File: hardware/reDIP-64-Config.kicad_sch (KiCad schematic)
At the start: 19 parts, among them J2 Conn_02x05_Odd_Even, SW1 KXT331LHS, U14 W957A8MFYA5I, U15 W25Q128JVPIM, U8 LFE5UM5G-25F-8MG285C

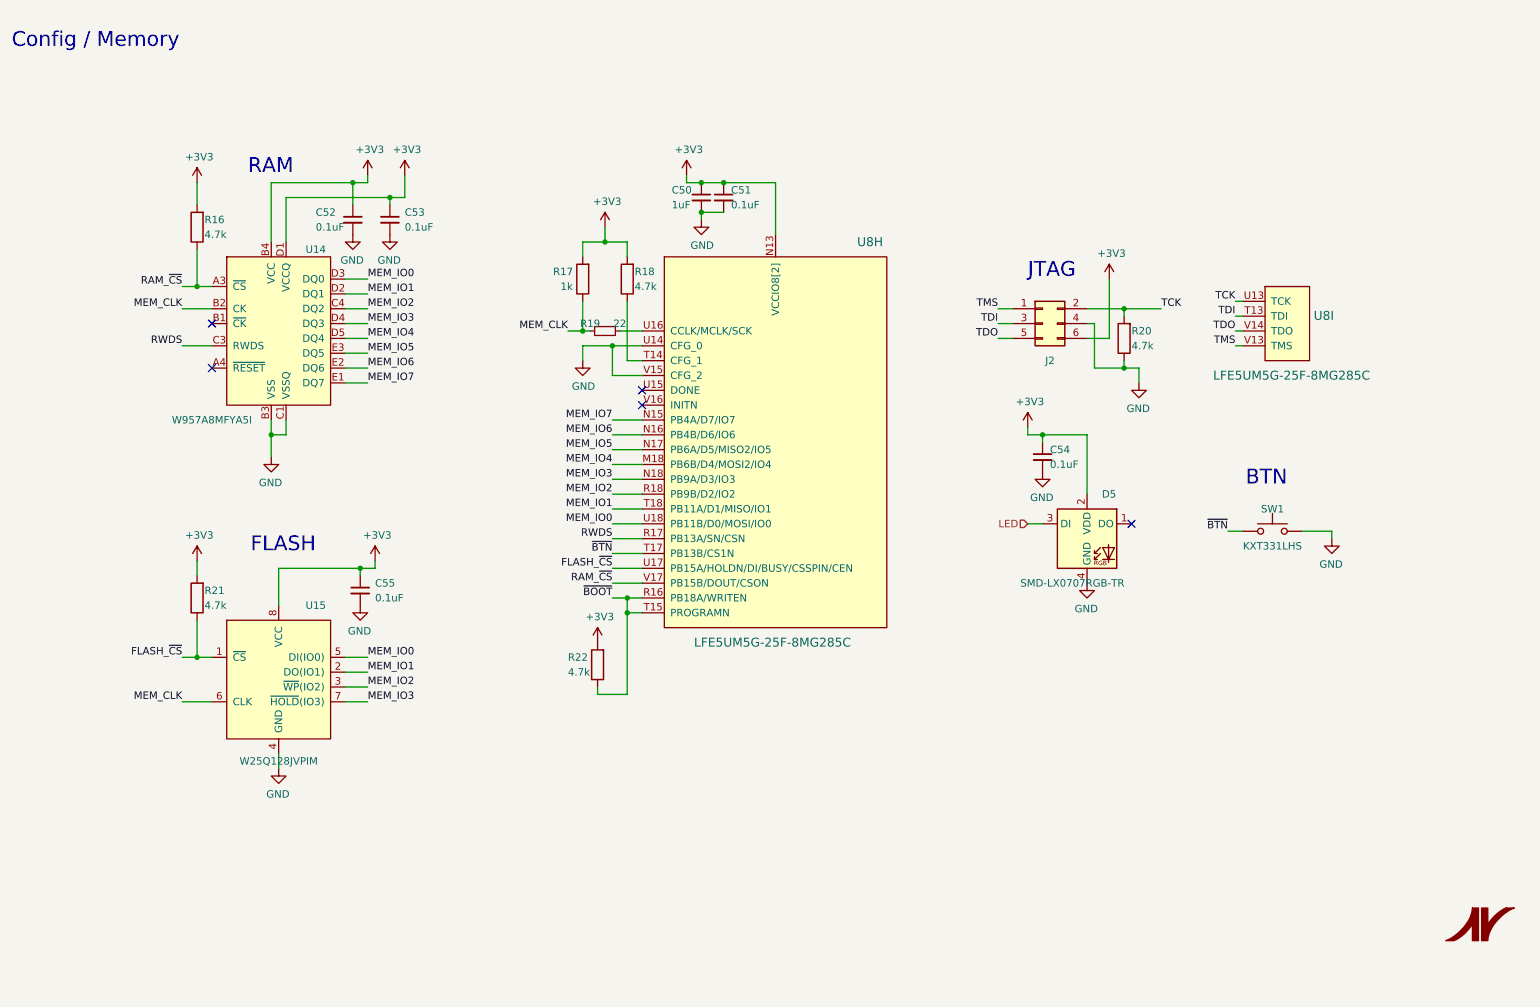
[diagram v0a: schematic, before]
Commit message: Various improvements
* Removed slash from sheet names
* Reannotated schematics
* Example derivation of clocks in schematics
* Identical capacitors for DisplayPort main lanes and AUX
* Replaced switch FSA2259UMX with FSUSB42UMX
* Modified PCB physical stackup to (hopefully) be manufacturable
* Only one microvia size (0.1mm)
* Changed track width for differential pairs
* Routing cleanups and improvements
* Added files for manufacture
* Updated README

Many thanks for advice and help go to @azonenberg, @DX-MON, @gatecat,
@smunaut, and @zyp.
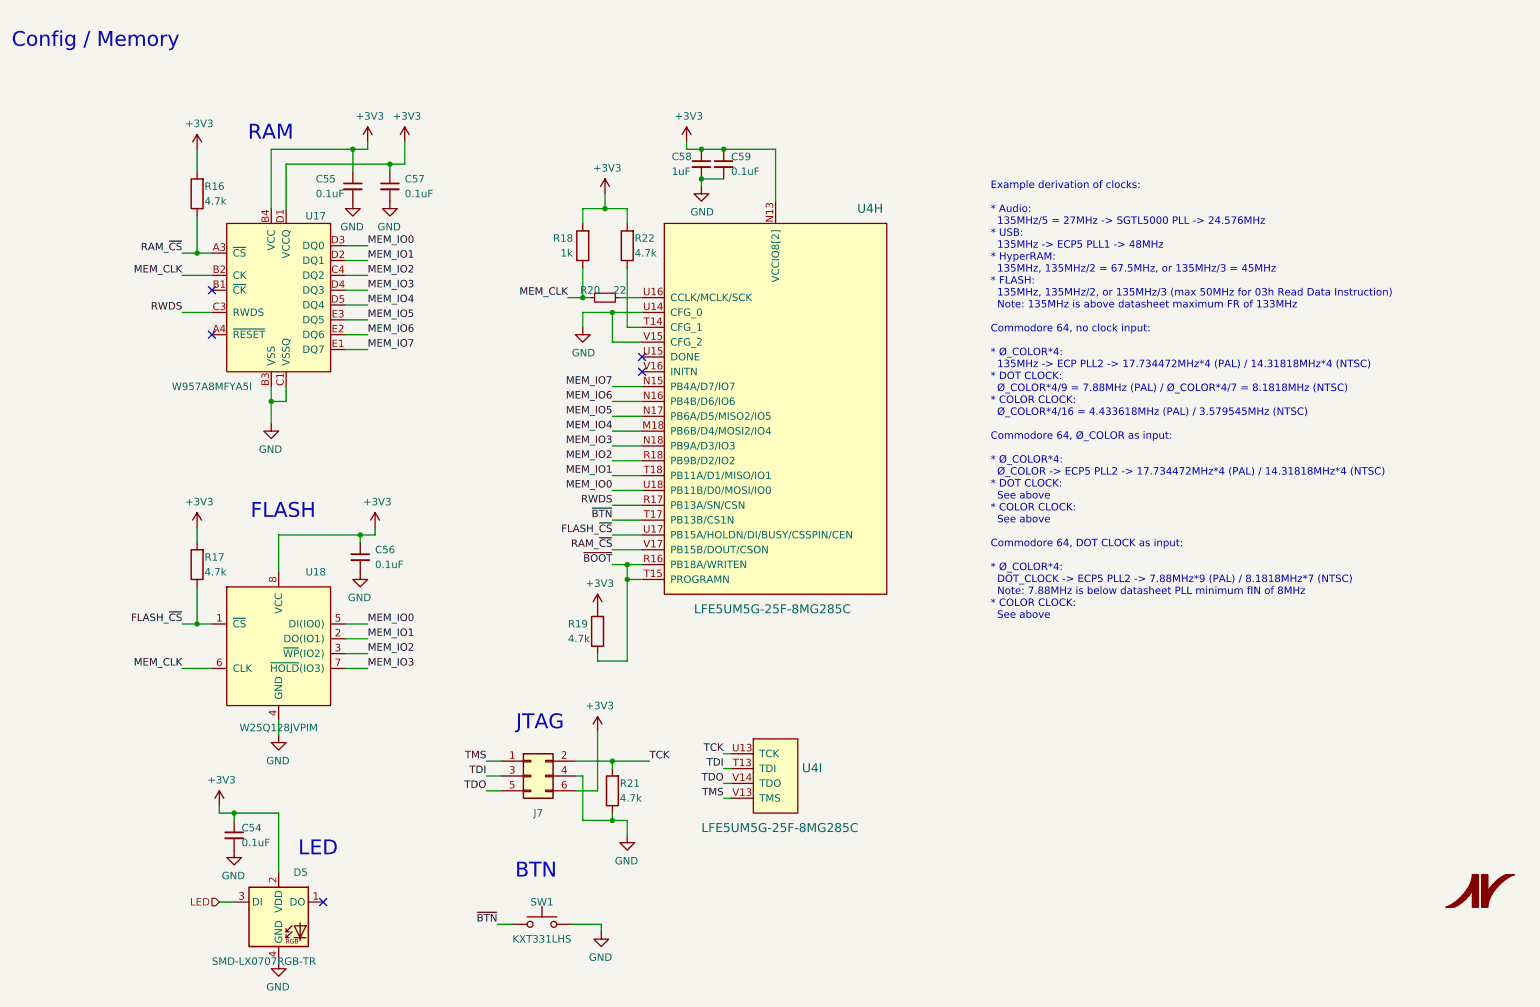
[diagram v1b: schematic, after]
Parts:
- renumbered C52 to C55, C55 to C56, C53 to C57, C50 to C58, C51 to C59, J2 to J7, R21 to R17, R17 to R18, R22 to R19, R19 to R20, R20 to R21, R18 to R22, U14 to U17, U15 to U18, U8 to U4
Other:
- note added: "Example derivation of clocks: * Audio: 135MHz/5 = 27MHz -> SGTL5000 PLL -> 24.576MHz * USB: 135MHz -> ECP5 PLL1 -> 48MHz * HyperRAM: 135MHz, 135MHz/2 = 67.5MHz, or 135MHz/3 = 45MHz * FLASH: 135MHz, 135MHz/2, or 135MHz/3 (max 50MHz for 03h Read Data Instruction) Note: 135MHz is above datasheet maximum FR of 133MHz Commodore 64, no clock input: * Ø_COLOR*4: 135MHz -> ECP PLL2 -> 17.734472MHz*4 (PAL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"
- note added: "LED"
- moved on the sheet: C54, C55, C56, C57, C58, C59, D5, J7, R16, R17, R18, R19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

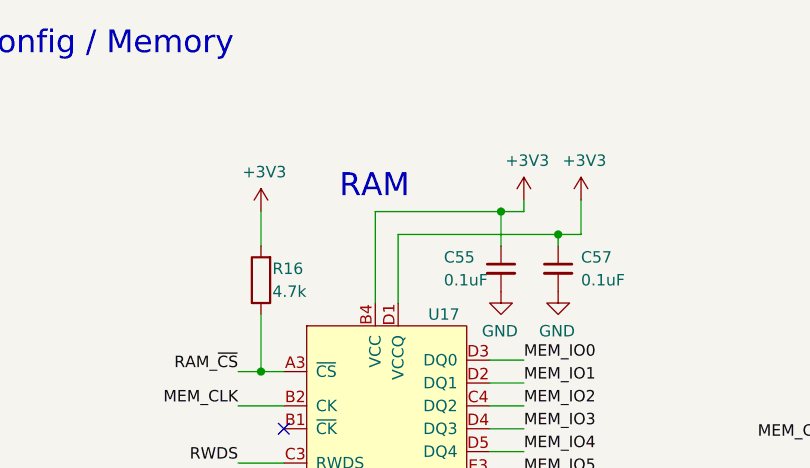
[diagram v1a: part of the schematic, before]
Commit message: Added stitching vias and test points
Thanks to @azonenberg for help and suggestions.
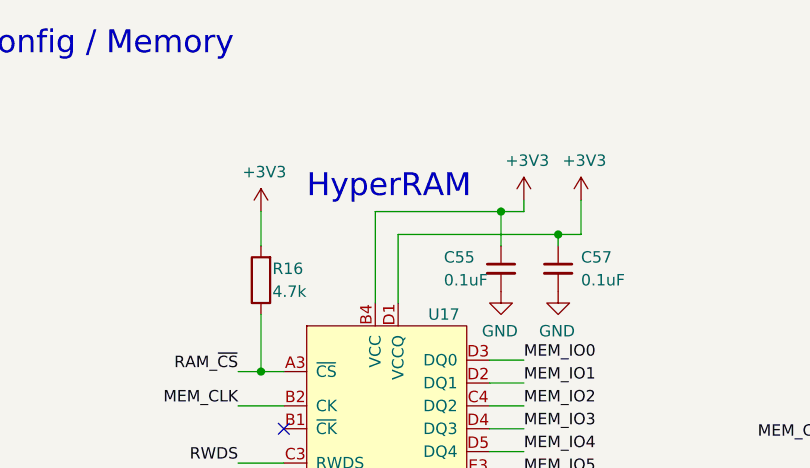
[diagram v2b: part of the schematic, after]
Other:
- note added: "HyperRAM"
- note removed: "RAM"
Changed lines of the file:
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@@
   (title_block
     (title "reDIP 64")
-    (date "2021-06-12")
+    (date "2021-06-16")
     (rev "0.2")
     (company "Nimrod")
@@
     (effects (font (size 2.54 2.54)) (justify left bottom))
   )
-  (text "RAM" (at 73.66 43.815 180)
-    (effects (font (size 2.54 2.54)) (justify right bottom))
+  (text "HyperRAM" (at 62.23 43.815 0)
+    (effects (font (size 2.54 2.54)) (justify left bottom))
   )
   (text "FLASH" (at 77.47 108.585 180)
@@
   (symbol (lib_id "power:+3V3") (at 57.15 45.085 0) (unit 1)
     (in_bom yes) (on_board yes)
-    (property "Reference" "#PWR0108" (id 0) (at 57.15 48.895 0)
+    (property "Reference" "#PWR0110" (id 0) (at 57.15 48.895 0)
       (effects (font (size 1.27 1.27)) hide)
     )
@@
   (symbol (lib_id "power:+3V3") (at 57.15 109.855 0) (unit 1)
     (in_bom yes) (on_board yes)
-    (property "Reference" "#PWR0109" (id 0) (at 57.15 113.665 0)
+    (property "Reference" "#PWR0111" (id 0) (at 57.15 113.665 0)
       (effects (font (size 1.27 1.27)) hide)
     )
@@
   (symbol (lib_id "power:+3V3") (at 60.96 157.48 0) (unit 1)
     (in_bom yes) (on_board yes)
-    (property "Reference" "#PWR0110" (id 0) (at 60.96 161.29 0)
+    (property "Reference" "#PWR0112" (id 0) (at 60.96 161.29 0)
       (effects (font (size 1.27 1.27)) hide)
     )
@@
   (symbol (lib_id "power:+3V3") (at 86.36 43.815 0) (unit 1)
     (in_bom yes) (on_board yes)
-    (property "Reference" "#PWR0117" (id 0) (at 86.36 47.625 0)
+    (property "Reference" "#PWR0119" (id 0) (at 86.36 47.625 0)
       (effects (font (size 1.27 1.27)) hide)
     )
@@
   (symbol (lib_id "power:+3V3") (at 87.63 109.855 0) (unit 1)
     (in_bom yes) (on_board yes)
-    (property "Reference" "#PWR0118" (id 0) (at 87.63 113.665 0)
+    (property "Reference" "#PWR0120" (id 0) (at 87.63 113.665 0)
       (effects (font (size 1.27 1.27)) hide)
     )
@@
   (symbol (lib_id "power:+3V3") (at 92.71 43.815 0) (unit 1)
     (in_bom yes) (on_board yes)
-    (property "Reference" "#PWR0120" (id 0) (at 92.71 47.625 0)
+    (property "Reference" "#PWR0122" (id 0) (at 92.71 47.625 0)
       (effects (font (size 1.27 1.27)) hide)
     )
@@
   (symbol (lib_id "power:+3V3") (at 125.73 123.825 0) (unit 1)
     (in_bom yes) (on_board yes)
-    (property "Reference" "#PWR0122" (id 0) (at 125.73 127.635 0)
+    (property "Reference" "#PWR0124" (id 0) (at 125.73 127.635 0)
       (effects (font (size 1.27 1.27)) hide)
     )
@@
   (symbol (lib_id "power:+3V3") (at 125.73 144.78 0) (unit 1)
     (in_bom yes) (on_board yes)
-    (property "Reference" "#PWR0123" (id 0) (at 125.73 148.59 0)
+    (property "Reference" "#PWR0125" (id 0) (at 125.73 148.59 0)
       (effects (font (size 1.27 1.27)) hide)
     )
@@
   (symbol (lib_id "power:+3V3") (at 127 52.705 0) (unit 1)
     (in_bom yes) (on_board yes)
-    (property "Reference" "#PWR0125" (id 0) (at 127 56.515 0)
+    (property "Reference" "#PWR0127" (id 0) (at 127 56.515 0)
       (effects (font (size 1.27 1.27)) hide)
     )
@@
   (symbol (lib_id "power:+3V3") (at 140.97 43.815 0) (unit 1)
     (in_bom yes) (on_board yes)
-    (property "Reference" "#PWR0127" (id 0) (at 140.97 47.625 0)
+    (property "Reference" "#PWR0129" (id 0) (at 140.97 47.625 0)
       (effects (font (size 1.27 1.27)) hide)
     )
@@
   (symbol (lib_id "power:GND") (at 63.5 165.1 0) (mirror y) (unit 1)
     (in_bom yes) (on_board yes)
-    (property "Reference" "#PWR0111" (id 0) (at 63.5 171.45 0)
+    (property "Reference" "#PWR0113" (id 0) (at 63.5 171.45 0)
       (effects (font (size 1.27 1.27)) hide)
     )
@@
   (symbol (lib_id "power:GND") (at 69.85 92.075 0) (mirror y) (unit 1)
     (in_bom yes) (on_board yes)
-    (property "Reference" "#PWR0112" (id 0) (at 69.85 98.425 0)
+    (property "Reference" "#PWR0114" (id 0) (at 69.85 98.425 0)
       (effects (font (size 1.27 1.27)) hide)
     )
@@
   (symbol (lib_id "power:GND") (at 71.12 145.415 0) (mirror y) (unit 1)
     (in_bom yes) (on_board yes)
-    (property "Reference" "#PWR0113" (id 0) (at 71.12 151.765 0)
+    (property "Reference" "#PWR0115" (id 0) (at 71.12 151.765 0)
       (effects (font (size 1.27 1.27)) hide)
     )
@@
   (symbol (lib_id "power:GND") (at 71.12 184.15 0) (mirror y) (unit 1)
     (in_bom yes) (on_board yes)
-    (property "Reference" "#PWR0114" (id 0) (at 71.12 190.5 0)
+    (property "Reference" "#PWR0116" (id 0) (at 71.12 190.5 0)
       (effects (font (size 1.27 1.27)) hide)
     )
@@
   (symbol (lib_id "power:GND") (at 83.82 53.975 0) (mirror y) (unit 1)
     (in_bom yes) (on_board yes)
-    (property "Reference" "#PWR0115" (id 0) (at 83.82 60.325 0)
+    (property "Reference" "#PWR0117" (id 0) (at 83.82 60.325 0)
       (effects (font (size 1.27 1.27)) hide)
     )
@@
   (symbol (lib_id "power:GND") (at 85.09 117.475 0) (mirror y) (unit 1)
     (in_bom yes) (on_board yes)
-    (property "Reference" "#PWR0116" (id 0) (at 85.09 123.825 0)
+    (property "Reference" "#PWR0118" (id 0) (at 85.09 123.825 0)
       (effects (font (size 1.27 1.27)) hide)
     )
@@
   (symbol (lib_id "power:GND") (at 90.17 53.975 0) (mirror y) (unit 1)
     (in_bom yes) (on_board yes)
-    (property "Reference" "#PWR0119" (id 0) (at 90.17 60.325 0)
+    (property "Reference" "#PWR0121" (id 0) (at 90.17 60.325 0)
       (effects (font (size 1.27 1.27)) hide)
     )
@@
   (symbol (lib_id "power:GND") (at 123.19 75.565 0) (unit 1)
     (in_bom yes) (on_board yes)
-    (property "Reference" "#PWR0121" (id 0) (at 123.19 81.915 0)
+    (property "Reference" "#PWR0123" (id 0) (at 123.19 81.915 0)
       (effects (font (size 1.27 1.27)) hide)
     )
@@
   (symbol (lib_id "power:GND") (at 126.365 179.07 0) (mirror y) (unit 1)
     (in_bom yes) (on_board yes)
-    (property "Reference" "#PWR0124" (id 0) (at 126.365 185.42 0)
+    (property "Reference" "#PWR0126" (id 0) (at 126.365 185.42 0)
       (effects (font (size 1.27 1.27)) hide)
     )
@@
   (symbol (lib_id "power:GND") (at 130.81 162.56 0) (mirror y) (unit 1)
     (in_bom yes) (on_board yes)
-    (property "Reference" "#PWR0126" (id 0) (at 130.81 168.91 0)
+    (property "Reference" "#PWR0128" (id 0) (at 130.81 168.91 0)
       (effects (font (size 1.27 1.27)) hide)
     )
@@
   (symbol (lib_id "power:GND") (at 143.51 51.435 0) (unit 1)
     (in_bom yes) (on_board yes)
-    (property "Reference" "#PWR0128" (id 0) (at 143.51 57.785 0)
-      (effects (font (size 1.27 1.27)) hide)
-    )
+    (property "Reference" "#PWR0130" (id 0) (at 143.51 57.785 0)
+      (effects (font (size 1.27 1.27)) hide)
+    )

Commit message: Updated all KiCad files to current format
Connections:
- net FLASH_~CS~ renamed FLASH_~{CS}
- net RAM_~CS~ renamed RAM_~{CS}
- net ~BOOT~ renamed ~{BOOT}
- net ~BTN~ renamed ~{BTN}
